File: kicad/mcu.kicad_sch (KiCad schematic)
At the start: 40 parts, among them J301 Debug, J302 Conn_01x03_Pin, Q301 GSF2301, Q302 2N7002, Q303 2N7002, SW301 SW_Push, U301 W25Q16JVSS, U302 RP2040, Y301 12Mhz

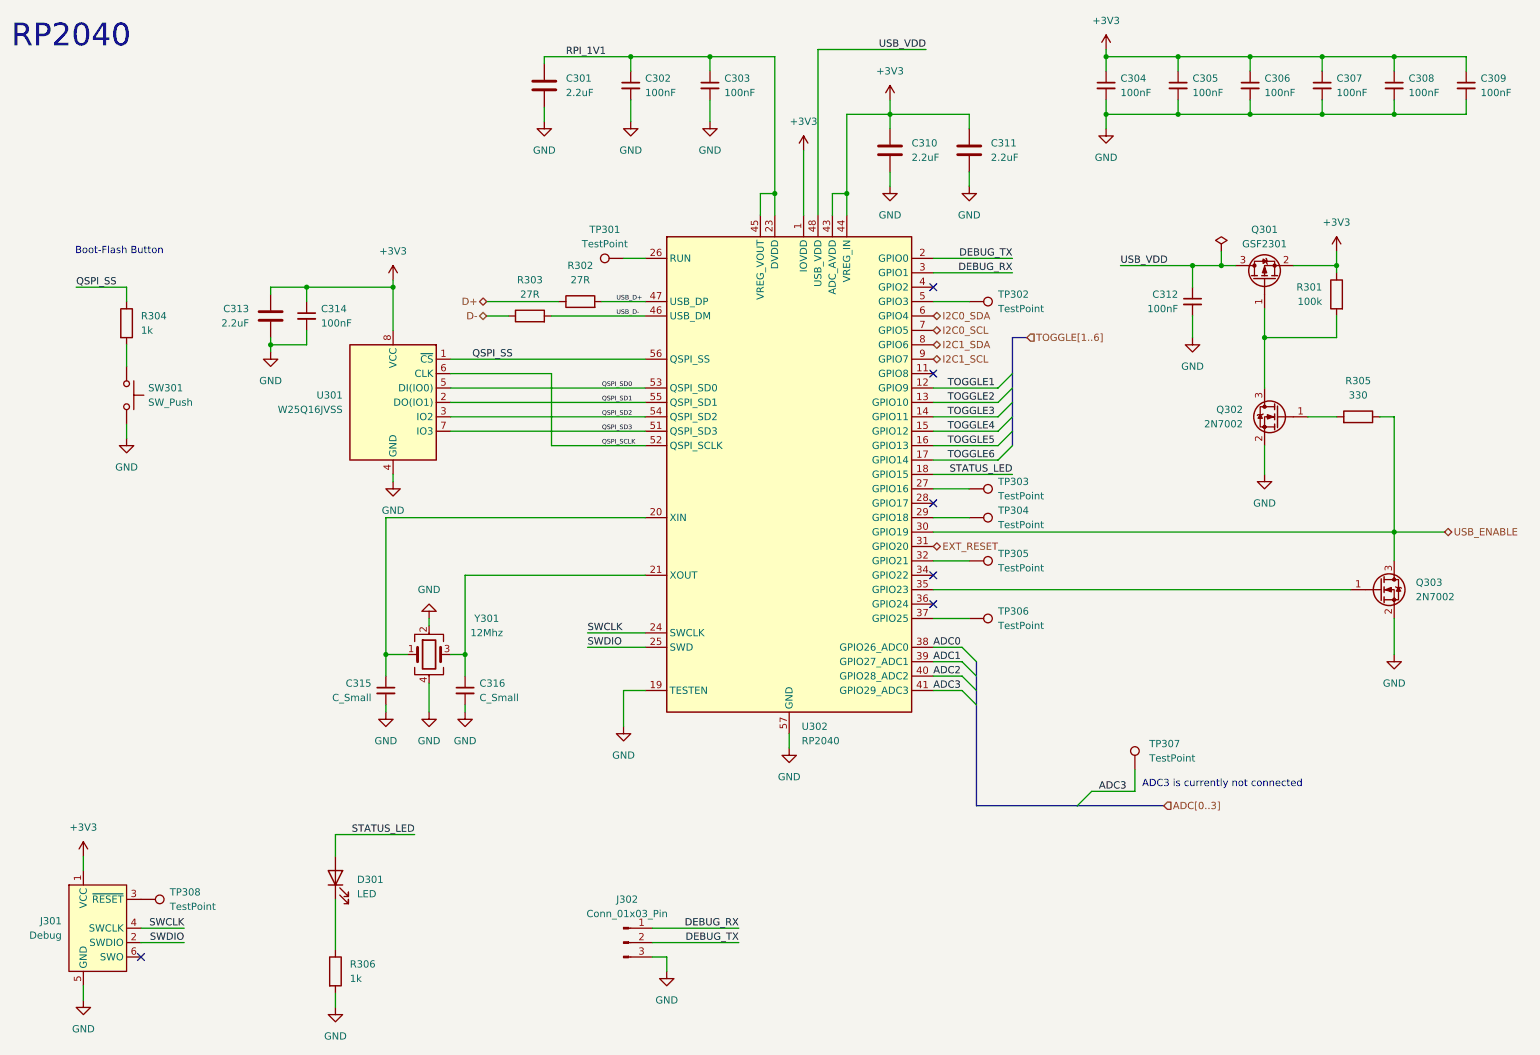
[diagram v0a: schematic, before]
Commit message: First rough placement
Just to get an idea on how it might look like
Added trace widts for Differential pairs
Using 6 layers, because it makes power management easier.
Rather large PCB, but better to big, then to small.
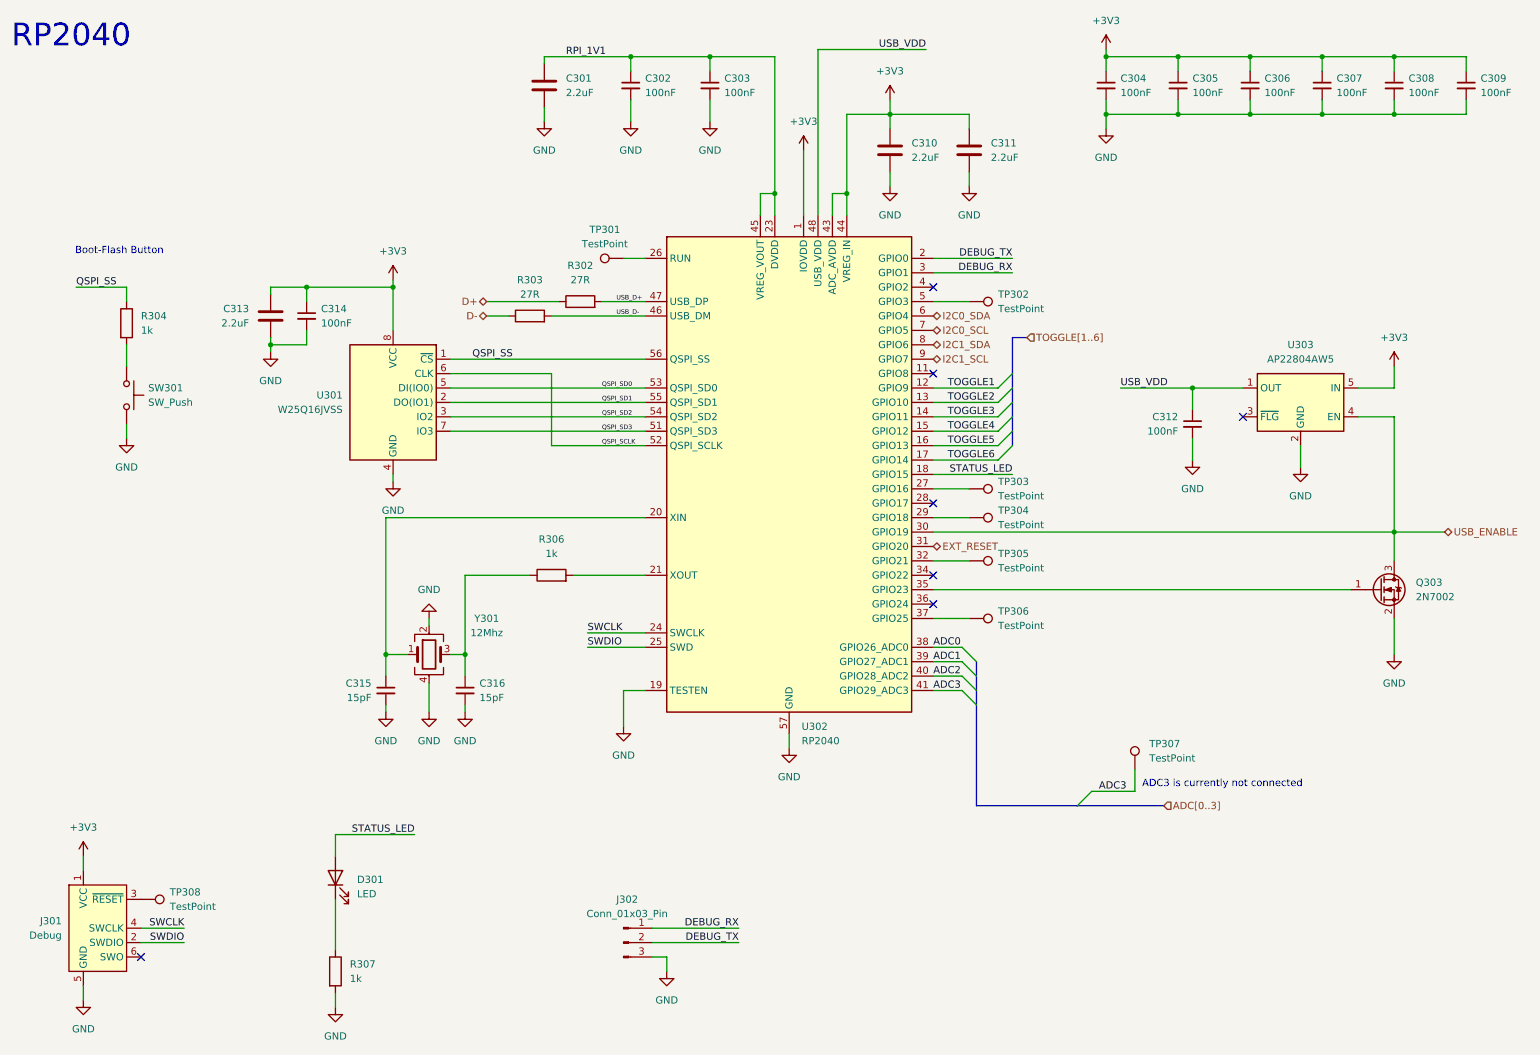
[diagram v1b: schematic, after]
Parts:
- removed Q301: GSF2301, Package_TO_SOT_SMD:SOT-23, symbol Transistor_FET:AO3401A
- removed Q302: 2N7002, Package_TO_SOT_SMD:SOT-23, symbol Transistor_FET:2N7002
- removed R301: 100k, Resistor_SMD:R_0603_1608Metric, symbol Device:R
- removed R305: 330, Resistor_SMD:R_0603_1608Metric, symbol Device:R
- added R306: 1k, Resistor_SMD:R_0603_1608Metric, symbol Device:R
- added U303: AP22804AW5, Package_TO_SOT_SMD:SOT-23-5, symbol Power_Management:AP22804AW5
- C315, C316: value C_Small -> 15pF
- Y301: footprint (none) -> Crystal:Crystal_SMD_3225-4Pin_3.2x2.5mm; PartNo (none) -> ABM8-272-T3
- renumbered R306 to R307
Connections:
- net +3V3: now also U303.5 (IN)
- net GND: now also U303.2 (GND)
- net USB_ENABLE: now also U303.4 (EN)
- net USB_VDD: now also U303.1 (OUT)
- net at C316.1, Y301.3: now also R306.1; no longer U302.21 (XOUT)
- new net: R306.2, U302.21 (XOUT)
- no-connect marks 6 -> 7
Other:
- moved on the sheet: C312

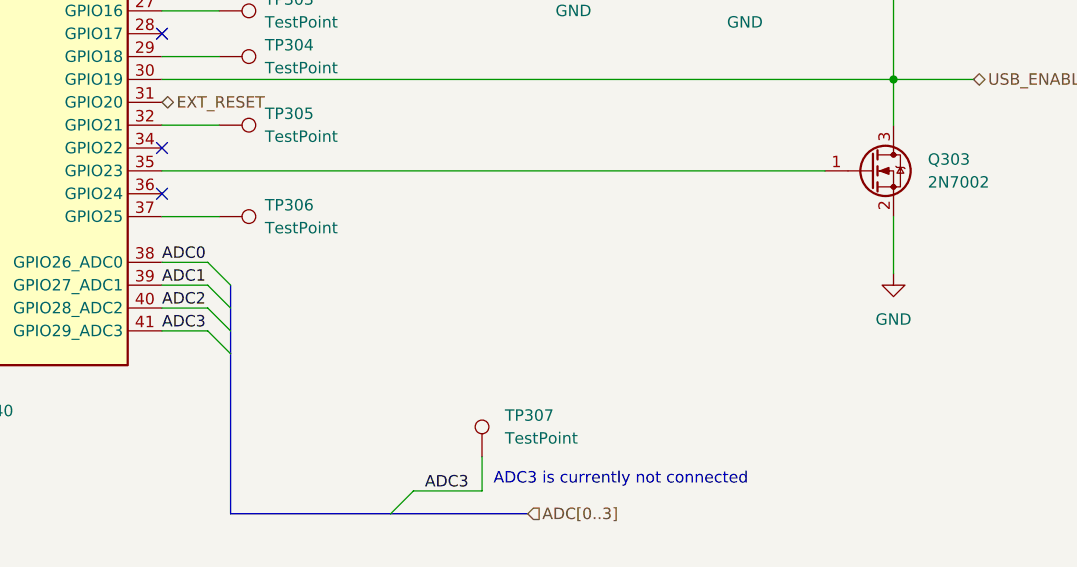
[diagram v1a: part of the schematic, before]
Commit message: Added first fanout for usb5807
Needs a lot more work, but it is a start, that allows me to concentrate
on the routing of USB signals and have the capacitors relatively close
to the hub controller.
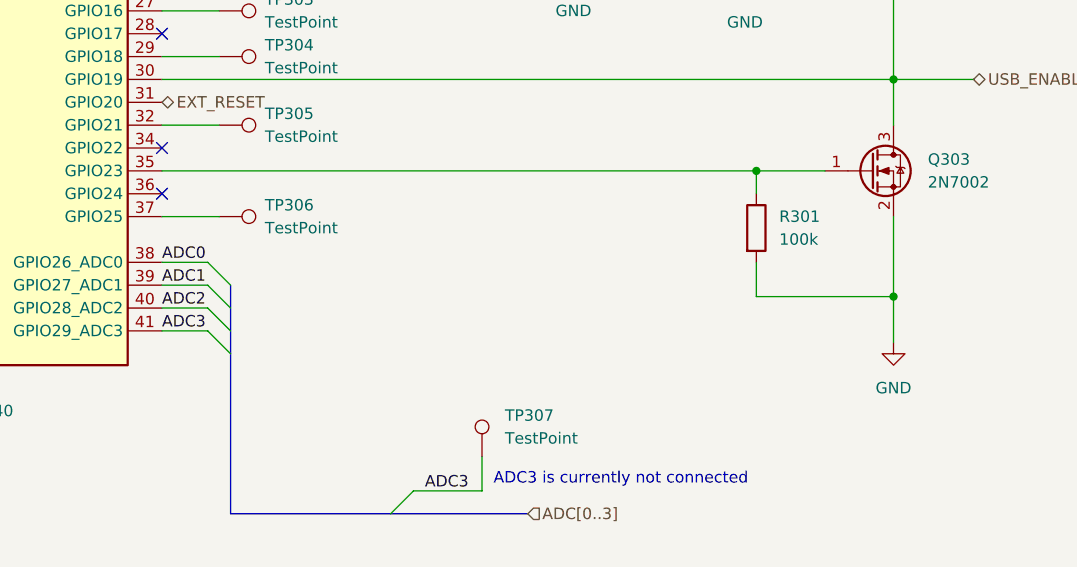
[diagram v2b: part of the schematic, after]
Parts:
- added R301: 100k, Resistor_SMD:R_0603_1608Metric, symbol Device:R
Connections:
- net GND: now also R301.2
- net at Q303.1 (G), U302.35 (GPIO23): now also R301.1
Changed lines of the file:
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@@
 	)
 	(junction
+		(at 257.81 128.27)
+		(diameter 0)
+		(color 0 0 0 0)
+	)
+	(junction
 		(at 257.81 30.48)
 		(diameter 0)
@@
 	)
 	(junction
+		(at 242.57 114.3)
+		(diameter 0)
+		(color 0 0 0 0)
+	)
+	(junction
 		(at 245.11 30.48)
 		(diameter 0)
@@
 	(wire
 		(pts
-			(xy 257.81 119.38) (xy 257.81 125.73)
+			(xy 257.81 119.38) (xy 257.81 128.27)
 		)
 		(stroke
@@
 	(wire
 		(pts
-			(xy 250.19 114.3) (xy 176.53 114.3)
+			(xy 250.19 114.3) (xy 242.57 114.3)
 		)
 		(stroke
@@
 	(wire
 		(pts
+			(xy 242.57 114.3) (xy 242.57 116.84)
+		)
+		(stroke
+			(width 0)
+			(type default)
+		)
+	)
+	(wire
+		(pts
 			(xy 109.22 88.9) (xy 125.73 88.9)
 		)
@@
 	(wire
 		(pts
+			(xy 242.57 128.27) (xy 257.81 128.27)
+		)
+		(stroke
+			(width 0)
+			(type default)
+		)
+	)
+	(wire
+		(pts
 			(xy 257.81 83.82) (xy 251.46 83.82)
 		)
@@
 	(wire
 		(pts
+			(xy 242.57 124.46) (xy 242.57 128.27)
+		)
+		(stroke
+			(width 0)
+			(type default)
+		)
+	)
+	(wire
+		(pts
 			(xy 146.05 44.45) (xy 148.59 44.45)
 		)
@@
 	(wire
 		(pts
+			(xy 257.81 128.27) (xy 257.81 133.35)
+		)
+		(stroke
+			(width 0)
+			(type default)
+		)
+	)
+	(wire
+		(pts
 			(xy 125.73 101.6) (xy 80.01 101.6)
 		)
@@
 	(wire
 		(pts
+			(xy 242.57 114.3) (xy 176.53 114.3)
+		)
+		(stroke
+			(width 0)
+			(type default)
+		)
+	)
+	(wire
+		(pts
 			(xy 257.81 20.32) (xy 257.81 22.86)
 		)
@@
 	(symbol
 		(lib_id "power:GND")
-		(at 257.81 125.73 0)
+		(at 257.81 133.35 0)
 		(unit 1)
 		(exclude_from_sim no)
@@
 		(fields_autoplaced yes)
 		(property "Reference" "#PWR0318"
-			(at 257.81 132.08 0)
+			(at 257.81 139.7 0)
 			(effects
 				(font
@@
 		)
 		(property "Value" "GND"
-			(at 257.81 130.81 0)
+			(at 257.81 138.43 0)
 			(effects
 				(font
@@
 		)
 		(property "Footprint" ""
-			(at 257.81 125.73 0)
+			(at 257.81 133.35 0)
 			(effects
 				(font
@@
 		)
 		(property "Datasheet" ""
-			(at 257.81 125.73 0)
+			(at 257.81 133.35 0)
 			(effects
 				(font
@@
 		)
 		(property "Description" "Power symbol creates a global label with name \"GND\" , ground"
-			(at 257.81 125.73 0)
+			(at 257.81 133.35 0)
 			(effects
 				(font
@@
 					(unit 1)
 				)
+			)
+		)
+	)
+	(symbol
+		(lib_id "Device:R")
+		(at 242.57 120.65 0)
+		(unit 1)
+		(exclude_from_sim no)
+		(in_bom yes)
+		(on_board yes)
+		(dnp no)
+		(fields_autoplaced yes)
+		(property "Reference" "R301"
+			(at 245.11 119.3799 0)
+			(effects
+				(font
+					(size 1.27 1.27)
+				)
+				(justify left)
+			)
+		)
+		(property "Value" "100k"
+			(at 245.11 121.9199 0)
+			(effects
+				(font
+					(size 1.27 1.27)
+				)
+				(justify left)
+			)
+		)
+		(property "Footprint" "Resistor_SMD:R_0603_1608Metric"
+			(at 240.792 120.65 90)
+			(effects
+				(font
+					(size 1.27 1.27)
+				)
+				(hide yes)
+			)
+		)
+		(property "Datasheet" "~"
+			(at 242.57 120.65 0)
+			(effects
+				(font
+					(size 1.27 1.27)
+				)
+				(hide yes)
+			)
+		)
+		(property "Description" "Resistor"
+			(at 242.57 120.65 0)
+			(effects
+				(font
+					(size 1.27 1.27)
+				)
+				(hide yes)
+			)
+		)
+		(pin "1"
+		)
+		(pin "2"
+		)
+		(instances
+			(project ""
+				(path "/fa2d0b8b-d66f-4d1f-bda6-9ad6b6242db5/e484743e-481f-4d37-adb3-d786ac2b08fb"
+					(reference "R301")
+					(unit 1)
+				)

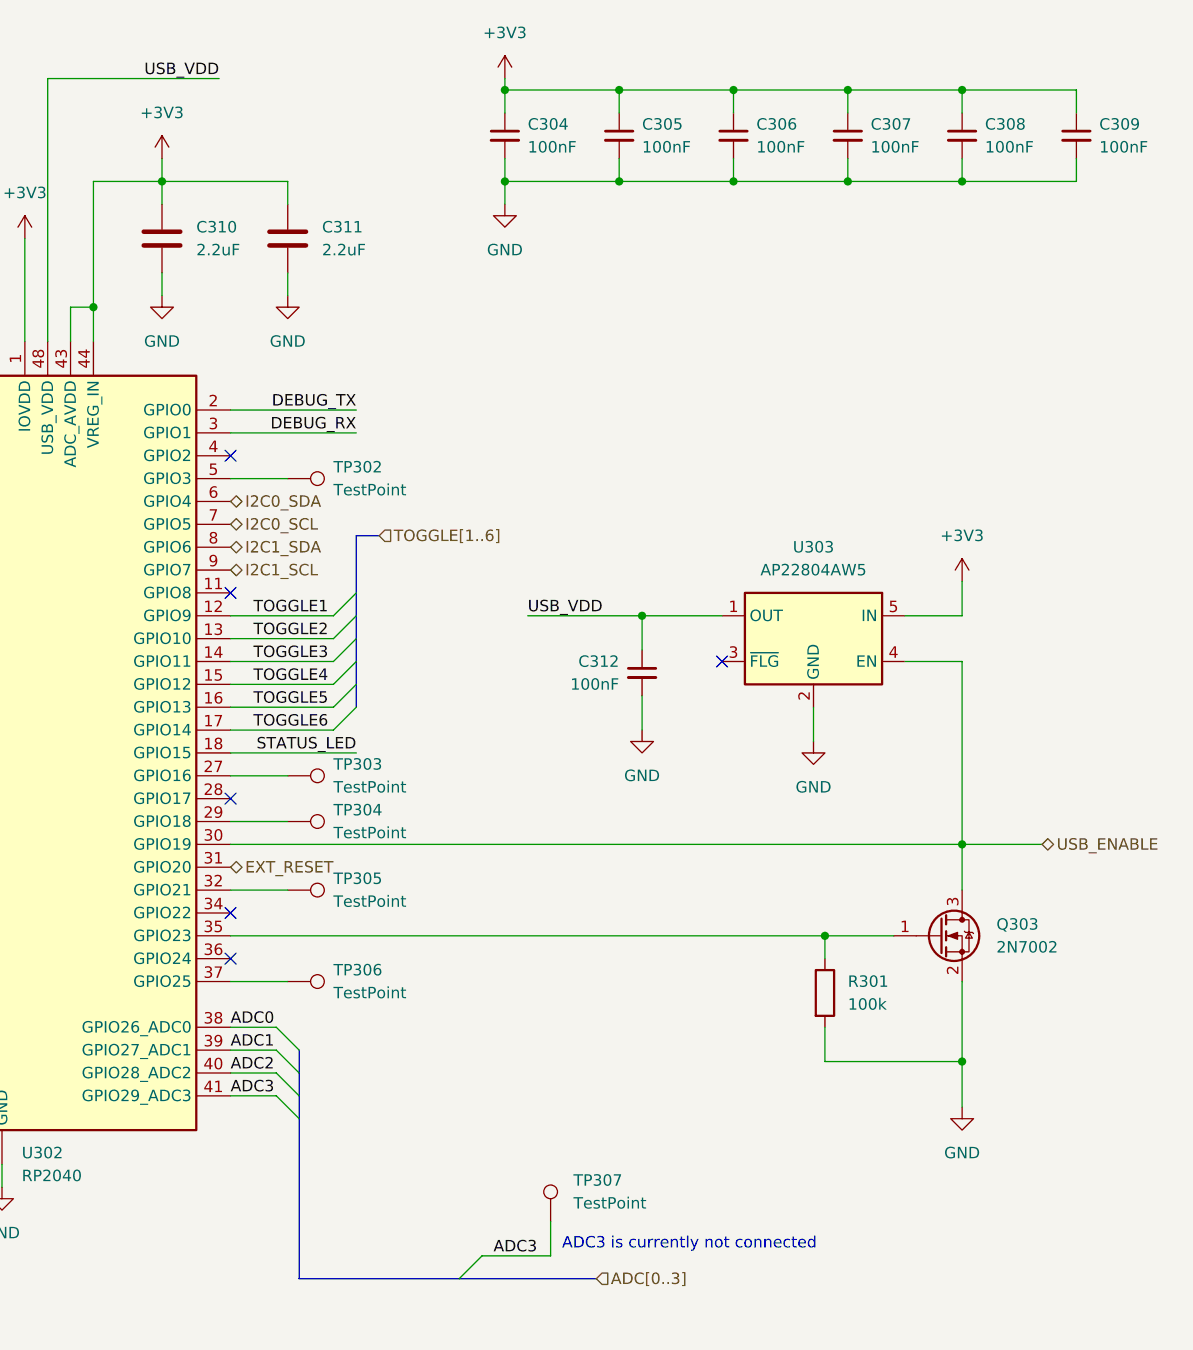
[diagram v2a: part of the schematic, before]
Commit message: Some more routing
Not done, but done some more. Nothing is final, just to get a
better feeling of what could be done.
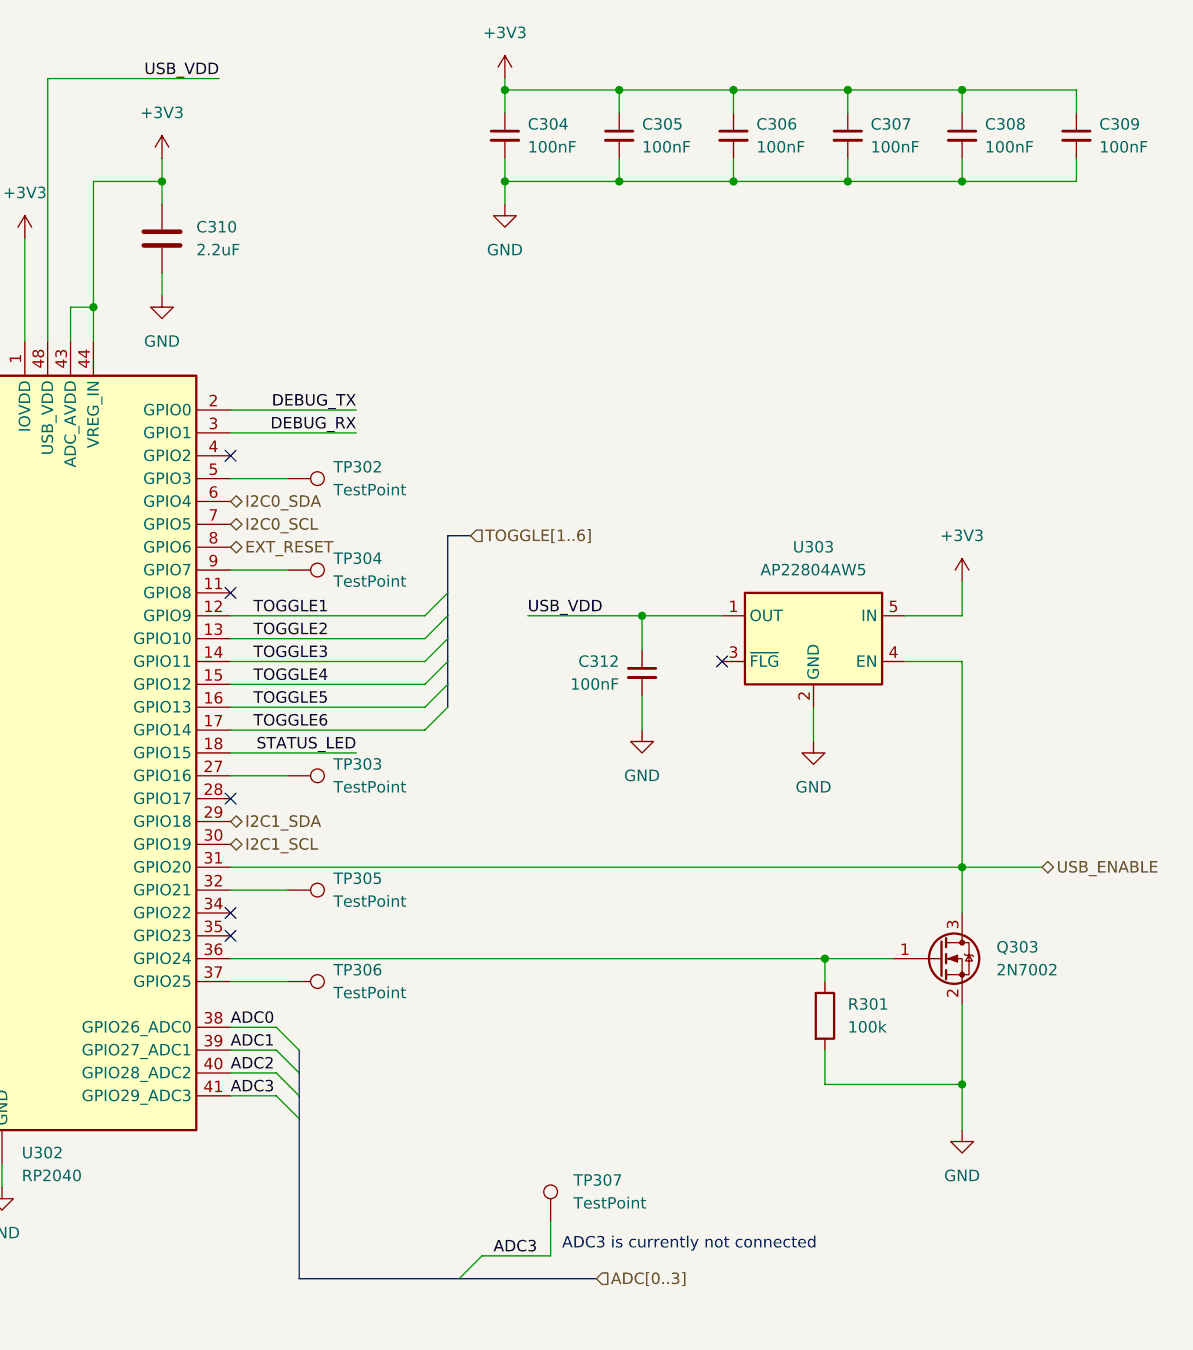
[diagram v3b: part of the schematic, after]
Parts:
- removed C311: 2.2uF, Capacitor_SMD:C_0603_1608Metric, symbol Device:C
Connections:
- net EXT_RESET: now also U302.8 (GPIO6); no longer U302.31 (GPIO20)
- net I2C1_SCL: now also U302.30 (GPIO19); no longer U302.9 (GPIO7)
- net I2C1_SDA: now also U302.29 (GPIO18); no longer U302.8 (GPIO6)
- net USB_ENABLE: now also U302.31 (GPIO20); no longer U302.30 (GPIO19)
- net at Q303.1 (G), R301.1: now also U302.36 (GPIO24); no longer U302.35 (GPIO23)
- net at TP304.1: now also U302.9 (GPIO7); no longer U302.29 (GPIO18)
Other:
- moved on the sheet: Q303, R301, TP304
